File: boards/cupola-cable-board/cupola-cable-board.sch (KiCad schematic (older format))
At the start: 13 parts, among them J1 LED, J2 ENC1, J3 ENC1, J4 ENC1, J5 ENC1, J6 ENC1, J7 ENC1

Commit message: [boards] Schematic fpr cupola cable board
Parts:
- removed JP1, JP2, JP3: GND_ENC1, Resistors_SMD:R_0603, symbol Jumper_NO_Small
- added C1, C2: 1u, Capacitor_SMD:C_0603_1608Metric, symbol Device:C
- added J10: MagnetEncoder2, Pin_Headers:Pin_Header_Straight_1x06_Pitch2.54mm, symbol cupola-cable-board-rescue:CONN_01X06
- added J8: MagnetEncoder0, Pin_Headers:Pin_Header_Straight_1x06_Pitch2.54mm, symbol cupola-cable-board-rescue:CONN_01X06
- added J9: MagnetEncoder1, Pin_Headers:Pin_Header_Straight_1x06_Pitch2.54mm, symbol cupola-cable-board-rescue:CONN_01X06
- added R1: 0, symbol Device:R
- added U1: TLV73333PDBV, Package_TO_SOT_SMD:SOT-23-5, symbol Regulator_Linear:TLV75533PDBV
- D1, D2, D3: symbol LED -> cupola-cable-board-rescue:LED
- J1: symbol CONN_01X02 -> cupola-cable-board-rescue:CONN_01X02
- J2: value ENC1 -> ENC0_OUT; symbol CONN_02X03 -> cupola-cable-board-rescue:CONN_02X03
- J3: value ENC1 -> ENC1_OUT; symbol CONN_02X03 -> cupola-cable-board-rescue:CONN_02X03
- J4: value ENC1 -> ENC2_OUT; symbol CONN_02X03 -> cupola-cable-board-rescue:CONN_02X03
- J5: value ENC1 -> Sensor0; symbol CONN_01X06 -> cupola-cable-board-rescue:CONN_01X06
- J6: value ENC1 -> Sensor1; symbol CONN_01X06 -> cupola-cable-board-rescue:CONN_01X06
- J7: value ENC1 -> Sensor2; symbol CONN_01X06 -> cupola-cable-board-rescue:CONN_01X06
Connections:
- net GND_ENC1 is gone; now on net GND: J2.2 (P2), J5.2 (P2)
- net GND: now also J6.2 (P2), J7.2 (P2), C1.2, C2.2, J10.2 (P2), J8.2 (P2), J9.2 (P2), U1.2 (GND)
- net 5V_ENC1 renamed +3V3
- net +3V3: now also J6.1 (P1), J7.1 (P1), C2.1, U1.5 (OUT); no longer J2.1 (P1)
- net 5V_ENC2: no longer names the net of J3.1 (P1)
- net 5V_ENC2: no longer J6.1 (P1)
- net 5V_ENC3: no longer names the net of J4.1 (P1)
- net 5V_ENC3: no longer J7.1 (P1)
- net A*_ENC1 renamed Differential_Drivers/Out0_A*
- net Differential_Drivers/Out0_A*: no longer J5.4 (P4)
- net A*_ENC2 renamed Differential_Drivers/Out1_A*
- net Differential_Drivers/Out1_A*: no longer J6.4 (P4)
- net A*_ENC3 renamed Differential_Drivers/Out2_A*
- net Differential_Drivers/Out2_A*: no longer J7.4 (P4)
- net A_ENC1 renamed Differential_Drivers/Out0_A
- net Differential_Drivers/Out0_A: no longer J5.3 (P3)
- net A_ENC2 renamed Differential_Drivers/Out1_A
- net Differential_Drivers/Out1_A: no longer J6.3 (P3)
- net A_ENC3 renamed Differential_Drivers/Out2_A
- net Differential_Drivers/Out2_A: no longer J7.3 (P3)
- net B*_ENC1 renamed Differential_Drivers/Out0_B*
- net Differential_Drivers/Out0_B*: no longer J5.6 (P6)
- net B*_ENC2 renamed Differential_Drivers/Out1_B*
- net Differential_Drivers/Out1_B*: no longer J6.6 (P6)
- net B*_ENC3 renamed Differential_Drivers/Out2_B*
- net Differential_Drivers/Out2_B*: no longer J7.6 (P6)
- net B_ENC1 renamed Differential_Drivers/Out0_B
- net Differential_Drivers/Out0_B: no longer J5.5 (P5)
- net B_ENC2 renamed Differential_Drivers/Out1_B
- net Differential_Drivers/Out1_B: no longer J6.5 (P5)
- net B_ENC3 renamed Differential_Drivers/Out2_B
- net Differential_Drivers/Out2_B: no longer J7.5 (P5)
- net GND_ENC2: no longer names the net of J3.2 (P2)
- net GND_ENC2: no longer J6.2 (P2)
- net GND_ENC3: no longer names the net of J4.2 (P2)
- net GND_ENC3: no longer J7.2 (P2)
- new net: C1.1, R1.1, U1.1 (IN), U1.3 (EN)
- new net +5V: J10.1 (P1), J2.1 (P1), J8.1 (P1), J9.1 (P1), R1.2
- new net Mag0_A: J8.3 (P3)
- new net Mag0_B: J8.5 (P5)
- new net Mag1_A: J9.3 (P3)
- new net Mag1_B: J9.5 (P5)
- new net Mag2_A: J10.3 (P3)
- new net Mag2_B: J10.5 (P5)
- new net Sensor0_Cs: J5.3 (P3)
- new net Sensor0_Motion: J5.4 (P4)
- new net Sensor0_Sck: J5.6 (P6)
- new net Sensor0_Sdio: J5.5 (P5)
- new net Sensor1_Cs: J6.3 (P3)
- new net Sensor1_Motion: J6.4 (P4)
- new net Sensor1_Sck: J6.6 (P6)
- new net Sensor1_Sdio: J6.5 (P5)
- new net Sensor2_Cs: J7.3 (P3)
- new net Sensor2_Motion: J7.4 (P4)
- new net Sensor2_Sck: J7.6 (P6)
- new net Sensor2_Sdio: J7.5 (P5)
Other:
- moved on the sheet: D1, D2, D3, J1, J2, J3, J4, J5, J6, J7

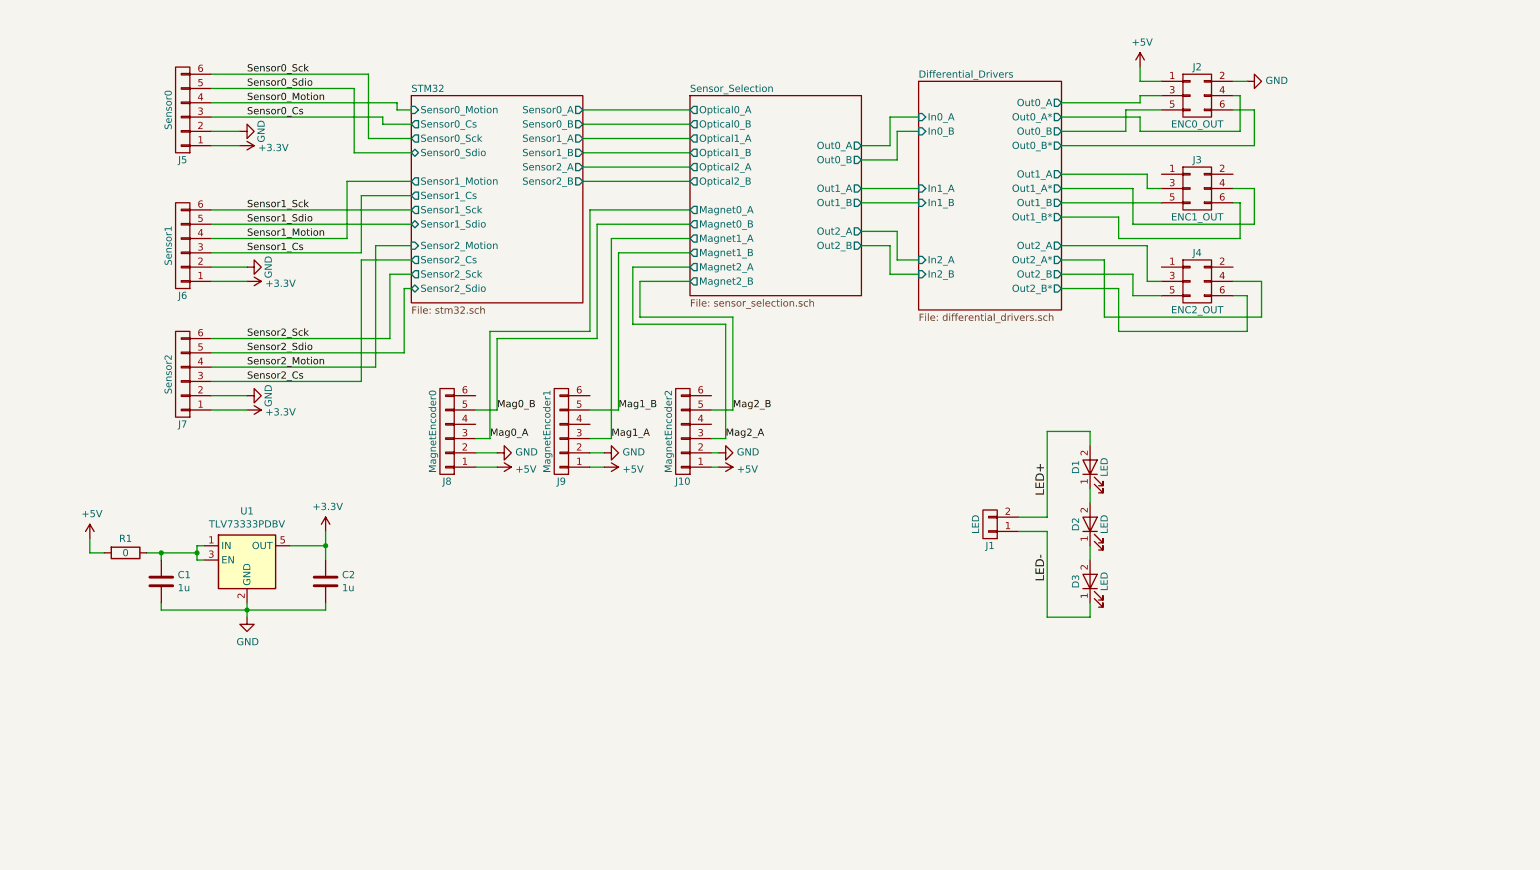
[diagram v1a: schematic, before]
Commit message: cupola_cable_board: 500mA 3.3V regulator, 4 pin connector for magnetic encoder
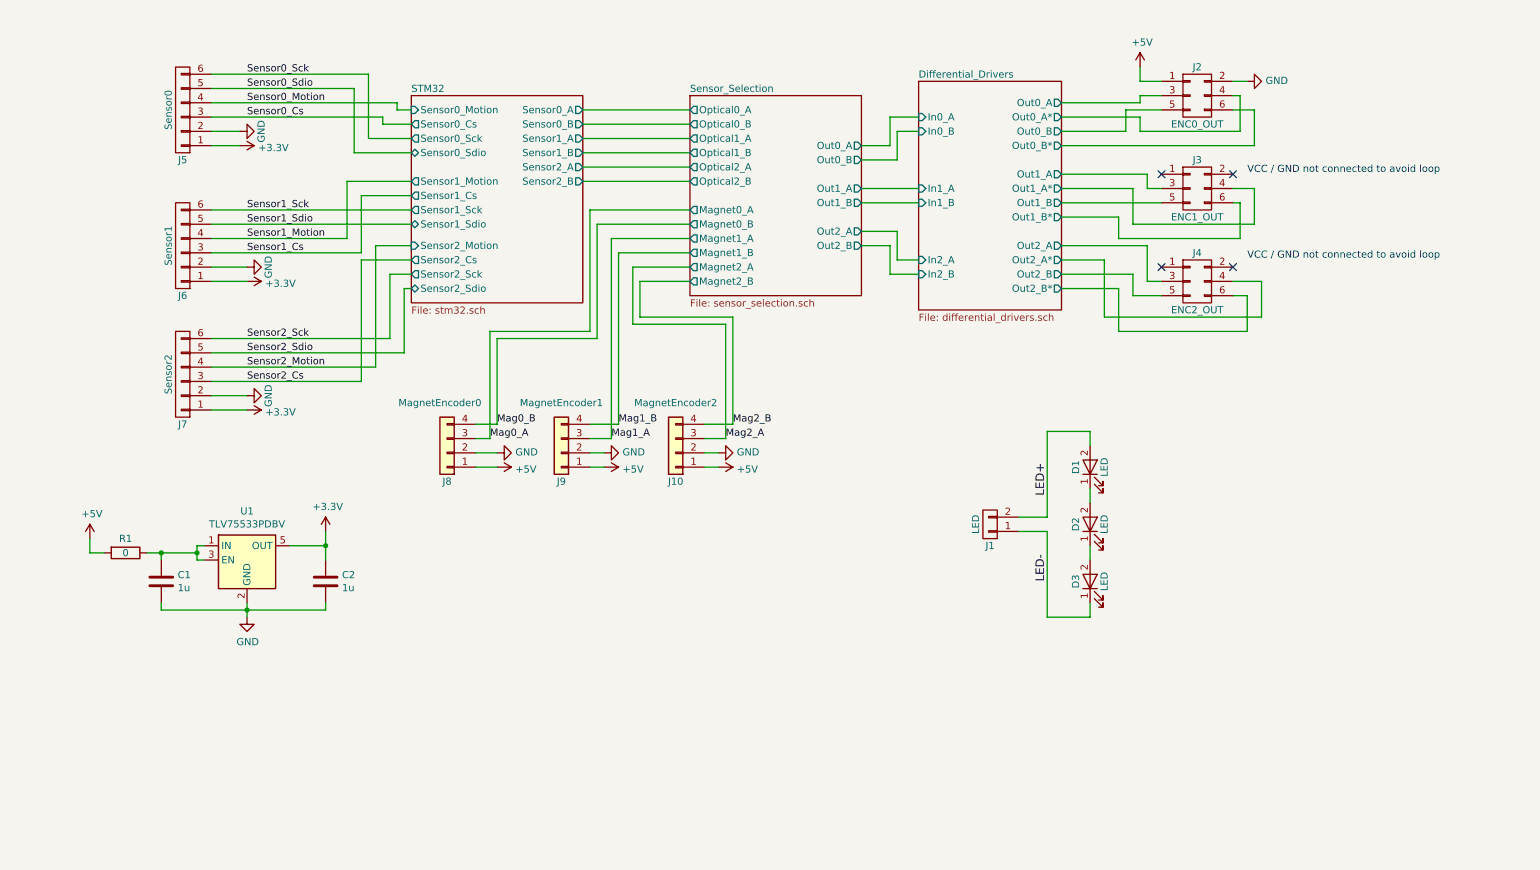
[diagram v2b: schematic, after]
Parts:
- removed J10: MagnetEncoder2, Pin_Headers:Pin_Header_Straight_1x06_Pitch2.54mm, symbol cupola-cable-board-rescue:CONN_01X06
- removed J8: MagnetEncoder0, Pin_Headers:Pin_Header_Straight_1x06_Pitch2.54mm, symbol cupola-cable-board-rescue:CONN_01X06
- removed J9: MagnetEncoder1, Pin_Headers:Pin_Header_Straight_1x06_Pitch2.54mm, symbol cupola-cable-board-rescue:CONN_01X06
- added J10: MagnetEncoder2, Connector_PinHeader_2.54mm:PinHeader_1x04_P2.54mm_Vertical, symbol Connector_Generic:Conn_01x04
- added J8: MagnetEncoder0, Connector_PinHeader_2.54mm:PinHeader_1x04_P2.54mm_Vertical, symbol Connector_Generic:Conn_01x04
- added J9: MagnetEncoder1, Connector_PinHeader_2.54mm:PinHeader_1x04_P2.54mm_Vertical, symbol Connector_Generic:Conn_01x04
- U1: value TLV73333PDBV -> TLV75533PDBV
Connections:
- net +5V: now also J10.1 (Pin_1), J8.1 (Pin_1), J9.1 (Pin_1)
- net GND: now also J10.2 (Pin_2), J8.2 (Pin_2), J9.2 (Pin_2)
- net Mag0_A: now also J8.3 (Pin_3)
- net Mag0_B: now also J8.4 (Pin_4)
- net Mag1_A: now also J9.3 (Pin_3)
- net Mag1_B: now also J9.4 (Pin_4)
- net Mag2_A: now also J10.3 (Pin_3)
- net Mag2_B: now also J10.4 (Pin_4)
- no-connect marks 0 -> 4
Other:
- note added: "VCC / GND not connected to avoid loop"
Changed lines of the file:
@@
 P 2250 4800
 F 0 "U1" H 2250 5142 50  0000 C CNN
-F 1 "TLV73333PDBV" H 2250 5051 50  0000 C CNN
+F 1 "TLV75533PDBV" H 2250 5051 50  0000 C CNN
 F 2 "Package_TO_SOT_SMD:SOT-23-5" H 2250 5100 50  0001 C CIN
 F 3 "http://www.ti.com/lit/ds/symlink/tlv755p.pdf" H 2250 4800 50  0001 C CNN
@@
 	1650 4750 1900 4750
 $Comp
-L cupola-cable-board-rescue:CONN_01X06 J8
-U 1 1 5C358FAB
-P 3650 3900
-F 0 "J8" H 3650 4250 50  0000 C CNN
-F 1 "MagnetEncoder0" V 3750 3900 50  0000 C CNN
-F 2 "Pin_Headers:Pin_Header_Straight_1x06_Pitch2.54mm" H 3650 3900 50  0001 C CNN
-F 3 "" H 3650 3900 50  0001 C CNN
-	1    3650 3900
-	-1   0    0    1
-$EndComp
-$Comp
-L cupola-cable-board-rescue:CONN_01X06 J9
-U 1 1 5C359059
-P 4450 3900
-F 0 "J9" H 4450 4250 50  0000 C CNN
-F 1 "MagnetEncoder1" V 4550 3900 50  0000 C CNN
-F 2 "Pin_Headers:Pin_Header_Straight_1x06_Pitch2.54mm" H 4450 3900 50  0001 C CNN
-F 3 "" H 4450 3900 50  0001 C CNN
-	1    4450 3900
-	-1   0    0    1
-$EndComp
-$Comp
-L cupola-cable-board-rescue:CONN_01X06 J10
-U 1 1 5C3590AF
-P 5300 3900
-F 0 "J10" H 5300 4250 50  0000 C CNN
-F 1 "MagnetEncoder2" V 5400 3900 50  0000 C CNN
-F 2 "Pin_Headers:Pin_Header_Straight_1x06_Pitch2.54mm" H 5300 3900 50  0001 C CNN
-F 3 "" H 5300 3900 50  0001 C CNN
-	1    5300 3900
-	-1   0    0    1
-$EndComp
-$Comp
 L power:+5V #PWR011
 U 1 1 5C35D921
@@
 	4750 4150 4650 4150
 Wire Wire Line
-	5550 4150 5500 4150
-Wire Wire Line
-	5550 4050 5500 4050
+	5550 4150 5450 4150
+Wire Wire Line
+	5550 4050 5450 4050
 Wire Wire Line
 	4750 4050 4650 4050
@@
 	3950 3950 3850 3950
 Wire Wire Line
-	3850 3750 4000 3750
-Wire Wire Line
-	4000 3750 4000 3250
+	3850 3850 4000 3850
+Wire Wire Line
+	4000 3850 4000 3250
 Wire Wire Line
 	4000 3250 4700 3250
@@
 	4800 2550 5350 2550
 Wire Wire Line
-	4650 3750 4850 3750
-Wire Wire Line
-	4850 3750 4850 2650
+	4650 3850 4850 3850
+Wire Wire Line
+	4850 3850 4850 2650
 Wire Wire Line
 	4850 2650 5350 2650
 Wire Wire Line
-	5500 3950 5600 3950
+	5450 3950 5600 3950
 Wire Wire Line
 	5600 3950 5600 3150
@@
 	5000 3100 5650 3100
 Wire Wire Line
-	5650 3100 5650 3750
-Wire Wire Line
-	5650 3750 5500 3750
+	5650 3100 5650 3850
+Wire Wire Line
+	5650 3850 5450 3850
 Text Label 3950 3950 0    50   ~ 0
 Mag0_A
-Text Label 4000 3750 0    50   ~ 0
+Text Label 4000 3850 0    50   ~ 0
 Mag0_B
 Text Label 4800 3950 0    50   ~ 0
 Mag1_A
-Text Label 5650 3750 0    50   ~ 0
+Text Label 5650 3850 0    50   ~ 0
 Mag2_B
 Text Label 5600 3950 0    50   ~ 0
 Mag2_A
-Text Label 4850 3750 0    50   ~ 0
+Text Label 4850 3850 0    50   ~ 0
 Mag1_B
 $Comp
@@
 Wire Wire Line
 	2000 3750 2250 3750
+$Comp
+L Connector_Generic:Conn_01x04 J8
+U 1 1 5C55F5CA
+P 3650 4050
+F 0 "J8" H 3650 4250 50  0000 C CNN
+F 1 "MagnetEncoder0" H 3700 3700 50  0000 C CNN
+F 2 "Connector_PinHeader_2.54mm:PinHeader_1x04_P2.54mm_Vertical" H 3650 4050 50  0001 C CNN
+F 3 "~" H 3650 4050 50  0001 C CNN
+	1    3650 4050
+	-1   0    0    1
+$EndComp
+NoConn ~ 9150 2100
+NoConn ~ 8650 2100
+NoConn ~ 8650 2750
+NoConn ~ 9150 2750
+Text Notes 9250 2100 0    50   ~ 0
+VCC / GND not connected to avoid loop
+Text Notes 9250 2700 0    50   ~ 0
+VCC / GND not connected to avoid loop
+$Comp
+L Connector_Generic:Conn_01x04 J9
+U 1 1 5C593AA0
+P 4450 4050
+F 0 "J9" H 4450 4250 50  0000 C CNN
+F 1 "MagnetEncoder1" H 4450 3700 50  0000 C CNN
+F 2 "Connector_PinHeader_2.54mm:PinHeader_1x04_P2.54mm_Vertical" H 4450 4050 50  0001 C CNN
+F 3 "~" H 4450 4050 50  0001 C CNN
+	1    4450 4050
+	-1   0    0    1
+$EndComp
+$Comp
+L Connector_Generic:Conn_01x04 J10
+U 1 1 5C5A3ABD
+P 5250 4050
+F 0 "J10" H 5250 4250 50  0000 C CNN
+F 1 "MagnetEncoder2" H 5250 3700 50  0000 C CNN
+F 2 "Connector_PinHeader_2.54mm:PinHeader_1x04_P2.54mm_Vertical" H 5250 4050 50  0001 C CNN
+F 3 "~" H 5250 4050 50  0001 C CNN
+	1    5250 4050
+	-1   0    0    1
+$EndComp
 $EndSCHEMATC

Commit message: cupola board: 2mm pin headers, led order
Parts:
- added C12, C13: 1u, Capacitor_SMD:C_0603_1608Metric, symbol Device:C
- added R7: 0, Resistor_SMD:R_0603_1608Metric, symbol Device:R
- added U3: TLV75533PDBV, Package_TO_SOT_SMD:SOT-23-5, symbol Regulator_Linear:TLV75533PDBV
- J1: footprint Pin_Headers:Pin_Header_Straight_1x02_Pitch2.54mm -> Connector_PinHeader_2.00mm:PinHeader_1x02_P2.00mm_Vertical
- J10, J8, J9: footprint Connector_PinHeader_2.54mm:PinHeader_1x04_P2.54mm_Vertical -> Connector_PinHeader_2.00mm:PinHeader_1x04_P2.00mm_Vertical
- J2, J3, J4: footprint Pin_Headers:Pin_Header_Straight_2x03_Pitch2.54mm -> Connector_PinHeader_2.00mm:PinHeader_2x03_P2.00mm_Vertical
- J5, J6, J7: footprint Pin_Headers:Pin_Header_Straight_1x06_Pitch2.54mm -> Connector_PinHeader_2.00mm:PinHeader_1x06_P2.00mm_Vertical
- R1: footprint (none) -> Resistor_SMD:R_0603_1608Metric
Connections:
- net labels added: +3.3VP
- wire segments 165 -> 183
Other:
- note added: "Second 3.3V rail (3V3)\nfor Sensor0, Sensor2"
- note added: "Separate supply rail +3V3\nfor Sensor0, Sensor2"
- moved on the sheet: D2, D3
